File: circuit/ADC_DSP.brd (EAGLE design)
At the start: 80 x 80 mm, 57 parts, among them IC1 REG1117, IC3 STM32F40XRXT6, IC4 CS4272, Q1 8MHz, Q2 24.576MHz

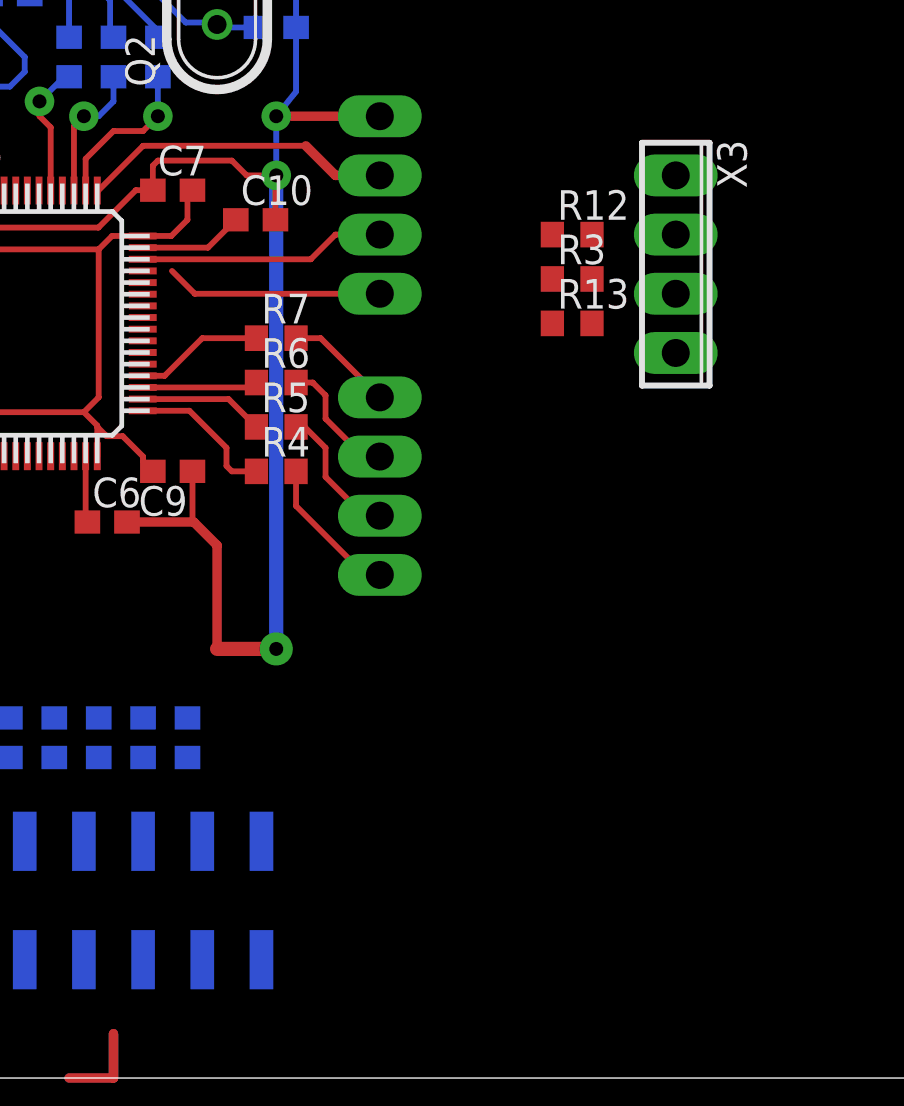
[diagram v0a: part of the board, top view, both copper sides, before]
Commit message: - добавили LCD разъем
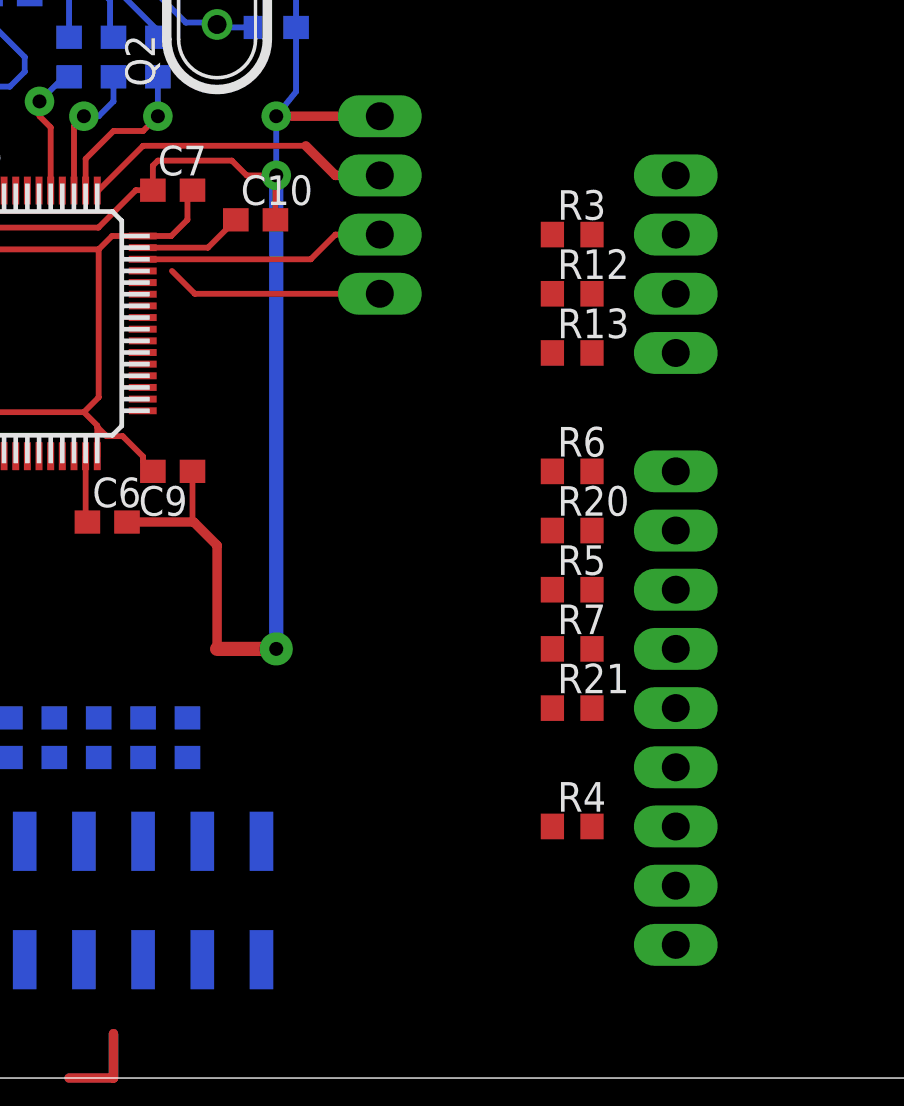
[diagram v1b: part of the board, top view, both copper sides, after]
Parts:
- removed SPI: (no value), con-phoenix-254:4POL254
- added LCD: (no value), con-phoenix-254:9POL254
- added R20, R21: 33, rcl:R0603
- moved R4 19.8 mm to (60.3, 10.8)
- moved R7 18.4 mm to (60.3, 18.4)
- moved R5 14.5 mm to (60.3, 21.0)
- moved R6 13.3 mm to (60.3, 26.0)
- moved R12 2.54 mm to (60.3, 33.7)
- moved R3 1.91 mm to (60.3, 36.2)
- moved R13 1.27 mm to (60.3, 31.1)
- flipped X3 to the bottom, turned to 90 degrees
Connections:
- net PB6 renamed PB6(AU_CCLK)
- net PB7 renamed PB7(AU_CDIN)
- net PB8 renamed PB8(AU_RST)
- net SPI2_MISO renamed PB14(TFT_MISO)
- net SPI2_MOSI renamed PB15(TFT_MOSI)
- net SPI2_NSS renamed PB12(TFT_CS)
- net SPI2_SCK renamed PB13(TFT_SCK)
- new net N$34: LCD.7, R4.2
- new net N$35: LCD.5, R21.2
- new net PC6(TFT_RESET): IC3.37, LCD.6
- new net PC7(TFT_D_C): IC3.38, R21.1
- new net PC8(TFT_LED): IC3.39, R20.1
- net +3V3: now also LCD.9
- net GND: now also LCD.8
- net N$20: now also LCD.1, R6.2; no longer R4.2, SPI.1
- net N$21: now also LCD.3; no longer SPI.2
- net N$22: now also LCD.2, R20.2; no longer R6.2, SPI.3
- net N$24: now also LCD.4; no longer SPI.4
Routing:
- net PB12(TFT_CS): track 6.41 -> 0.00 mm
- net N$20: track 6.31 -> 0.00 mm
- net N$21: track 5.91 -> 0.00 mm
- net PB15(TFT_MOSI): track 5.55 -> 0.00 mm
- net N$22: track 5.50 -> 0.00 mm
- net PB13(TFT_SCK): track 5.37 -> 0.00 mm
- net PB14(TFT_MISO): track 4.97 -> 0.00 mm
- net N$24: track 4.65 -> 0.00 mm

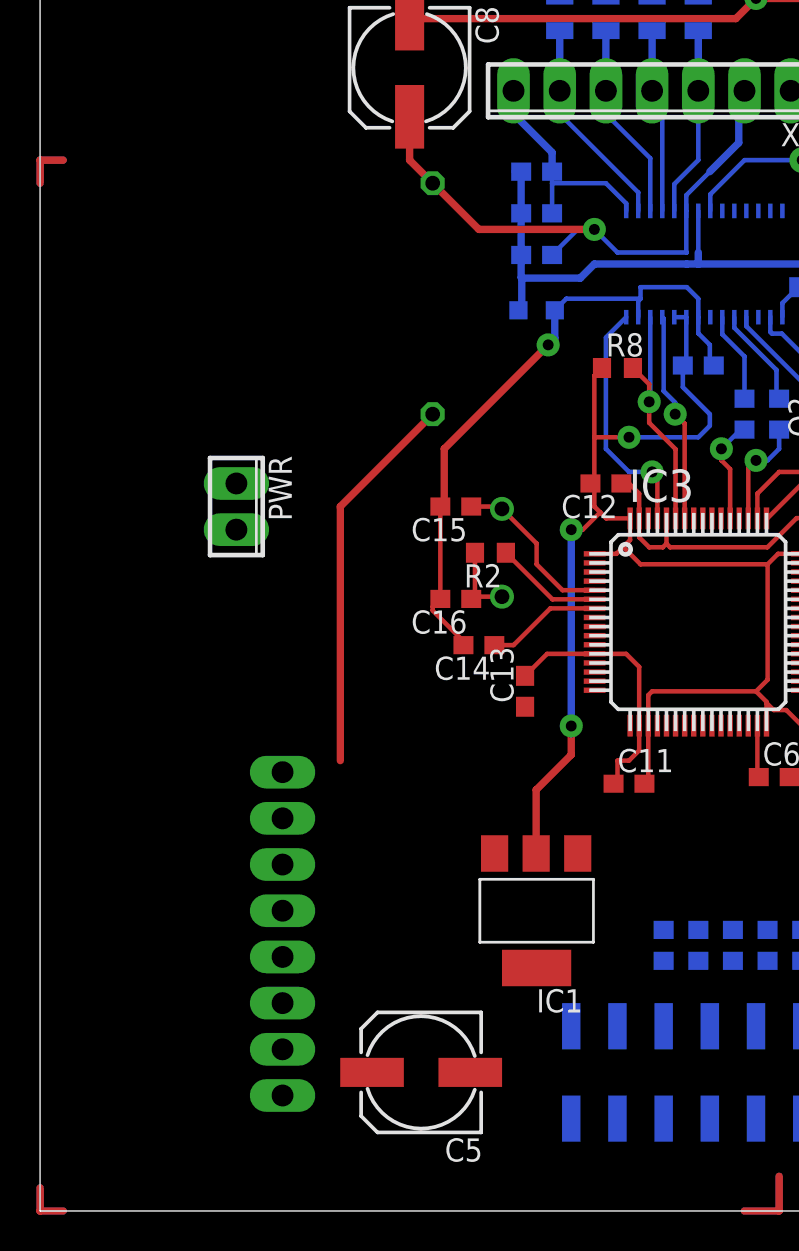
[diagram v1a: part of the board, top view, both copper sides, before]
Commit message: - добавил 4 GPIO
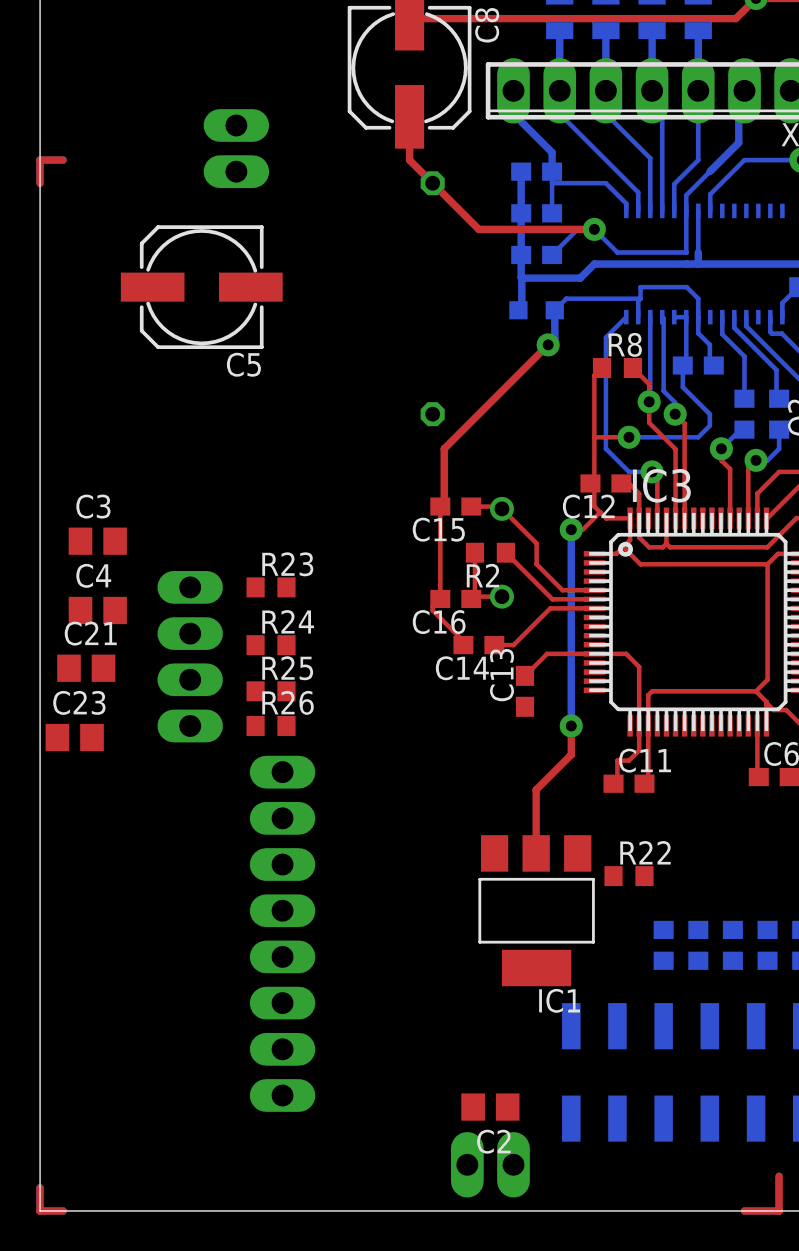
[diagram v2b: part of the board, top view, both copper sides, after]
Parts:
- added C2: 470p, rcl:C0805
- added C21, C23, C3, C4: 1n, rcl:C0805
- added DAC: (no value), con-phoenix-254:2POL254
- added GPIO: (no value), con-phoenix-254:4POL254
- added R22: 22k, rcl:R0603
- added R23, R24, R25, R26: 1.5k, rcl:R0603
- moved C5 44.8 mm to (8.89, 50.8)
- moved PWR 19.7 mm to (10.8, 58.4), flipped to the bottom, turned to 90 degrees
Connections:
- net USB_ON renamed PA10(USB_ON)
- new net N$36: IC3.20, R22.2
- new net N$37: C2.1, DAC.1, R22.1
- new net N$38: C3.1, GPIO.1, R23.1
- new net N$39: C4.1, GPIO.2, R24.1
- new net N$40: C21.1, GPIO.3, R25.1
- new net N$41: C23.1, GPIO.4, R26.1
- new net PC0(GPIO): IC3.8, R23.2
- new net PC1(GPIO): IC3.9, R24.2
- new net PC2(GPIO): IC3.10, R25.2
- new net PC3(GPIO): IC3.11, R26.2
- net GND: now also C2.2, C21.2, C23.2, C3.2, C4.2, DAC.2
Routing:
- net +5V: track 21.2 -> 0.00 mm

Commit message: - развели еще немного
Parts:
- removed C13: 0.1u, rcl:C0603
- moved IC1 31.0 mm to (15.2, 45.1), turned to 90 degrees
- moved DAC 22.9 mm to (25.4, 25.4)
- moved C2 16.6 mm to (26.0, 22.2)
- moved C23 7.01 mm to (8.89, 26.7), turned to 180 degrees
- moved C21 6.38 mm to (8.89, 29.2), turned to 180 degrees
- moved C3 6.25 mm to (8.89, 34.3), turned to 180 degrees
- moved C5 6.02 mm to (6.99, 45.1), turned to 90 degrees
- moved C4 5.85 mm to (8.89, 31.8), turned to 180 degrees
- moved C16 5.43 mm to (24.8, 38.7), turned to 90 degrees
- moved C15 5.08 mm to (27.9, 38.7), turned to 90 degrees
- moved GPIO 5.08 mm to (13.3, 30.5)
- moved C14 4.96 mm to (21.0, 34.9), turned to 90 degrees
- moved R25 4.49 mm to (17.1, 29.2)
- moved R23 4.45 mm to (17.1, 34.3)
- moved R26 4.45 mm to (17.1, 26.7)
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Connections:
- net +3V3: no longer C13.1
- net GND: no longer C13.2
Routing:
- net GND: track 124.5 -> 246.0 mm, vias 4 -> 7
- net +3V3: track 95.2 -> 142.7 mm
- net PC6(TFT_RESET): track 0.00 -> 36.7 mm, vias 0 -> 2
- net PA7: track 0.00 -> 31.2 mm
- net PC7(TFT_D_C): track 0.00 -> 30.6 mm, vias 0 -> 2
- net PA6: track 0.00 -> 29.4 mm
- net PB12(TFT_CS): track 0.00 -> 28.1 mm
- net PA5: track 0.00 -> 27.6 mm
- net PB15(TFT_MOSI): track 0.00 -> 27.3 mm, vias 0 -> 2
- net PC8(TFT_LED): track 0.00 -> 24.3 mm, vias 0 -> 2
- net PA2: track 0.00 -> 23.0 mm
- net PB13(TFT_SCK): track 0.00 -> 21.0 mm
- net PA1: track 0.00 -> 20.8 mm
- net PA0: track 0.00 -> 20.0 mm
- net PB14(TFT_MISO): track 0.00 -> 19.1 mm
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
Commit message: - развели в первом приближении
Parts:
- removed X3: (no value), con-phoenix-254:4POL254
- added USB: (no value), con-phoenix-254:3POL254
- moved C5 17.7 mm to (11.4, 62.2), turned to 0 degrees
- moved SWD 5.75 mm to (52.7, 43.2)
- moved PWR 4.49 mm to (11.4, 54.0), turned to 0 degrees
- moved R12 2.54 mm to (60.3, 36.2)
- moved R3 2.41 mm to (60.3, 33.8)
- moved IC1 0.90 mm to (15.9, 45.7), turned to 180 degrees
- moved R8 0.64 mm to (31.1, 46.4), flipped to the bottom, turned to 180 degrees
- moved R13 0.38 mm to (60.3, 31.5)
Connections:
- net GND: now also USB.3; no longer X3.4
- net N$16: now also USB.1; no longer X3.2
- net N$3: now also USB.2; no longer X3.3
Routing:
- net GND: track 246.0 -> 376.5 mm
- net +3V3: track 142.7 -> 187.7 mm, vias 3 -> 5
- net PA10(USB_ON): track 0.00 -> 18.5 mm
- net USB_DP: track 0.00 -> 18.2 mm
- net USB_DM: track 0.00 -> 17.7 mm
- net +5V: track 0.00 -> 17.2 mm
- net N$16: track 0.00 -> 9.37 mm
- net SWDIO: track 10.6 -> 15.8 mm
- net N$3: track 0.00 -> 4.07 mm
- net SWDCLK: track 13.4 -> 17.2 mm
- net N$35: track 0.00 -> 3.59 mm
- net N$24: track 0.00 -> 3.59 mm
- net N$22: track 0.00 -> 3.59 mm
- net N$21: track 0.00 -> 3.59 mm
- net N$20: track 0.00 -> 3.59 mm
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
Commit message: - развели вход для CS4272
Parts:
- removed X4: (no value), con-phoenix-254:7POL254
- added C13, C25, C31, C32, C33, C34, C35, C36: 2.2u, rcl:C0603
- added IC2: 74HC4052D, 40xx:SO16
- added INA: (no value), con-phoenix-254:4POL254
- added INB: PIN8X2, balmer:PIN8X2_SMD
- added R27, R28, R29, R30: 1.2k, rcl:R0603
- added R31, R32, R33, R34: 10k, rcl:R0603
- C27, C28: value (none) -> 1.5n
- C29, C30: value (none) -> 2.2u; device rcl:C0805 -> rcl:C0603
- moved C30 146.0 mm to (-6.35, -73.7), flipped to the top, turned to 0 degrees
- moved C29 140.4 mm to (-6.35, -68.6), flipped to the top, turned to 0 degrees
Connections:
- removed net AINA+: C28.1, IC4.17, X4.5
- removed net N$38: C3.1, GPIO.1, R23.1
- removed net N$39: C4.1, GPIO.2, R24.1
- new net 4052_A: C3.1, GPIO.1, IC2.10, R23.1
- new net 4052_B: C4.1, GPIO.2, IC2.9, R24.1
- new net N$13: C13.2, INB.P$1
- new net N$26: C34.2, INB.P$15
- new net N$28: C32.1, IC2.5
- new net N$30: C31.1, IC2.1
- new net N$42: C30.1, IC2.11
- new net N$43: C29.1, IC2.15
- new net N$44: C25.1, IC2.14
- new net N$45: C13.1, IC2.12
- new net N$46: IC2.13, R27.2, R33.2
- new net N$47: IC2.3, R28.2, R34.2
- new net N$48: C28.2, IC4.16, R30.1
- new net N$49: C25.2, INB.P$3
- new net N$50: C35.1, R29.2, R32.2
- new net N$51: C36.1, R30.2, R31.2
- new net N$52: C29.2, INB.P$5
- new net N$53: C31.2, INB.P$9
- new net N$54: C33.2, INB.P$13
- new net N$55: C34.1, IC2.4
- new net N$56: C33.1, IC2.2
- new net N$57: C32.2, INB.P$11
- new net N$58: C30.2, INB.P$7
- new net N$59: C35.2, INA.1
- new net N$60: C36.2, INA.4
- net AGND: now also IC2.6, IC2.7, IC2.8, INA.2, INA.3, INB.P$10, INB.P$12, INB.P$14, INB.P$16, INB.P$2, INB.P$4, INB.P$6, INB.P$8; no longer C27.2, C28.2, C29.2, C30.2, X4.1
- net AINB+: now also C27.2, R28.1; no longer C29.1, X4.4
- net AVCC: now also IC2.16; no longer X4.2
- net N$15: now also C27.1, R27.1; no longer C30.1, X4.3
- net N$18: now also C28.1, IC4.17, R29.1; no longer C27.1, IC4.16, X4.6
- net VCOM: now also R31.1, R32.1, R33.1, R34.1; no longer X4.7
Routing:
- net AGND: track 91.0 -> 78.8 mm
- net N$18: track 11.9 -> 0.00 mm
- net AINA+: track 11.1 -> 0.00 mm
- net N$15: track 10.6 -> 3.34 mm
- net N$39: track 6.48 -> 0.00 mm
- net 4052_B: track 0.00 -> 6.48 mm
- net N$38: track 6.46 -> 0.00 mm
- net 4052_A: track 0.00 -> 6.46 mm
- net AVCC: track 32.9 -> 27.0 mm
- net AINB+: track 10.3 -> 6.05 mm
- net VCOM: track 12.6 -> 11.3 mm

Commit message: - перед заменой на более быстрый мультиплексор.
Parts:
- removed C29, C30, C31, C32, C33, C34: 2.2u, rcl:C0603
- moved C36 174.3 mm to (28.6, 66.7), flipped to the bottom, turned to 90 degrees
- moved C35 170.2 mm to (32.4, 66.7), flipped to the bottom, turned to 90 degrees
- moved C25 133.5 mm to (41.9, 61.0), flipped to the bottom, turned to 180 degrees
- moved C13 131.7 mm to (41.9, 64.1), flipped to the bottom, turned to 180 degrees
- moved INA 129.1 mm to (29.8, 71.1), flipped to the bottom
- moved R34 121.8 mm to (37.5, 66.0), flipped to the bottom, turned to 180 degrees
- moved R33 119.5 mm to (37.5, 68.6), flipped to the bottom
- moved R32 103.4 mm to (27.3, 60.3), flipped to the bottom, turned to 180 degrees
- moved R31 101.0 mm to (27.3, 62.9), flipped to the bottom, turned to 180 degrees
- moved R30 96.2 mm to (30.5, 61.6), flipped to the bottom, turned to 90 degrees
- moved R29 92.6 mm to (33.0, 61.6), flipped to the bottom, turned to 90 degrees
- moved INB 90.3 mm to (61.6, 62.9), flipped to the bottom, turned to 180 degrees
- moved R28 89.2 mm to (35.6, 61.6), flipped to the bottom, turned to 90 degrees
- moved R27 86.0 mm to (38.1, 61.6), flipped to the bottom, turned to 90 degrees
- moved IC2 83.0 mm to (47.6, 67.3), flipped to the bottom, turned to 90 degrees
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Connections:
- removed net N$49: C25.2, INB.P$3
- removed net N$52: C29.2, INB.P$5
- removed net N$53: C31.2, INB.P$9
- removed net N$54: C33.2, INB.P$13
- removed net N$55: C34.1, IC2.4
- removed net N$56: C33.1, IC2.2
- removed net N$57: C32.2, INB.P$11
- removed net N$58: C30.2, INB.P$7
- new net N$38: IC2.2, INB.P$13
- new net N$39: C25.1, R28.2, R34.2
- net N$13: now also C25.2, IC2.3; no longer C13.2, INB.P$1
- net N$26: now also IC2.4; no longer C34.2
- net N$28: now also C13.1, R27.2, R33.2; no longer C32.1, IC2.5
- net N$30: now also C13.2, IC2.13; no longer C31.1, IC2.1
- net N$42: now also IC2.5, INB.P$11; no longer C30.1, IC2.11
- net N$43: now also IC2.1, INB.P$9; no longer C29.1, IC2.15
- net N$44: now also IC2.11, INB.P$7; no longer C25.1, IC2.14
- net N$45: now also IC2.15, INB.P$5; no longer C13.1, IC2.12
- net N$46: now also IC2.14, INB.P$3; no longer IC2.13, R27.2, R33.2
- net N$47: now also IC2.12, INB.P$1; no longer IC2.3, R28.2, R34.2
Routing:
- net AGND: track 78.8 -> 41.6 mm, vias 2 -> 0
- net N$50: track 0.00 -> 10.4 mm
- net N$48: track 0.00 -> 6.75 mm
- net N$18: track 0.00 -> 6.24 mm
- net N$51: track 0.00 -> 5.63 mm
- net N$15: track 3.34 -> 8.21 mm
- net N$60: track 0.00 -> 4.65 mm
- net N$59: track 0.00 -> 4.12 mm
- net VCOM: track 11.3 -> 13.7 mm
- net AVCC: track 27.0 -> 24.9 mm
- net N$12: track 18.8 -> 18.7 mm, vias 1 -> 0
